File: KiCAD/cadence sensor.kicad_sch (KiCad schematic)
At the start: 42 parts, among them J1 USB_C_Receptacle_USB2.0_16P, J2 JST_BATT, J4 JST_SOL, SW1 SW_Push, SW2 SW_PWR, U1 ESP32-S3-WROOM-1-N4, U2 TPD4E05U06DQA, U7 BQ25570

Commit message: KiCAD use local modified of footprint for JST connector
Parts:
- J2, J4: footprint JST2:JST_XH_S2B-XH-A-1_1x02_P2.50mm_Horizontal_2 -> Connector_JST:JST_XH_S2B-XH-A-1_1x02_P2.50mm_Horizontal
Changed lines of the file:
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@@
 			)
 		)
-		(property "Footprint" "JST2:JST_XH_S2B-XH-A-1_1x02_P2.50mm_Horizontal_2"
+		(property "Footprint" "Connector_JST:JST_XH_S2B-XH-A-1_1x02_P2.50mm_Horizontal"
 			(at 33.02 152.4 0)
 			(effects
@@
 			)
 		)
-		(property "Footprint" "JST2:JST_XH_S2B-XH-A-1_1x02_P2.50mm_Horizontal_2"
+		(property "Footprint" "Connector_JST:JST_XH_S2B-XH-A-1_1x02_P2.50mm_Horizontal"
 			(at 29.21 138.43 0)
 			(effects

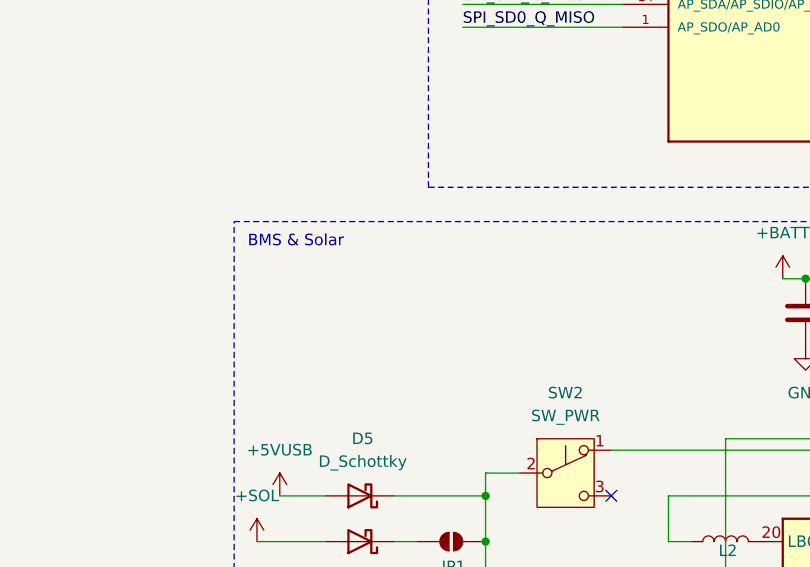
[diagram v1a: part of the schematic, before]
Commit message: found issue in PCB design
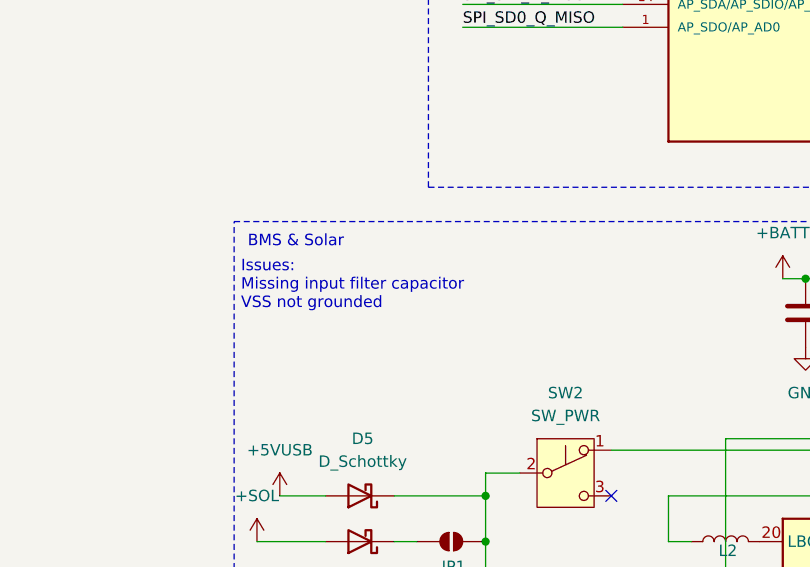
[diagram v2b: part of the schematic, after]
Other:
- note added: "Issues: Missing input filter capacitor VSS not grounded"
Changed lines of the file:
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@@
+		)
+	)
+	(text "Issues:\nMissing input filter capacitor\nVSS not grounded\n"
+		(exclude_from_sim no)
+		(at 156.972 80.772 0)
+		(effects
+			(font
+				(size 1.27 1.27)
+			)
+			(justify left)
 		)
 	)
